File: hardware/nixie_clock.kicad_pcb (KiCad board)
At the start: 2 copper layers, 224 x 70 mm, 98 parts, among them J1 Conn_02x02_Odd_Even, J2 USB_C_Receptacle_USB2.0_16P, J7 Barrel_Jack_Switch, Q1 IRF740, Q2 BSS138, Q3 BSS138, Q4 BSS138, Q5 BSS138, Q6 BSS138, Q8 BSS138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

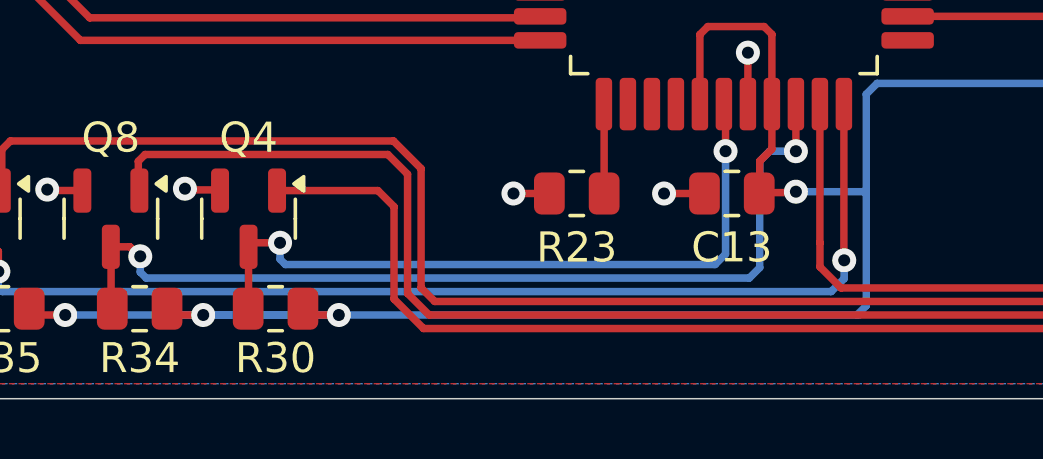
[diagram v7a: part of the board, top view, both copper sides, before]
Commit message: Correct track near U5.
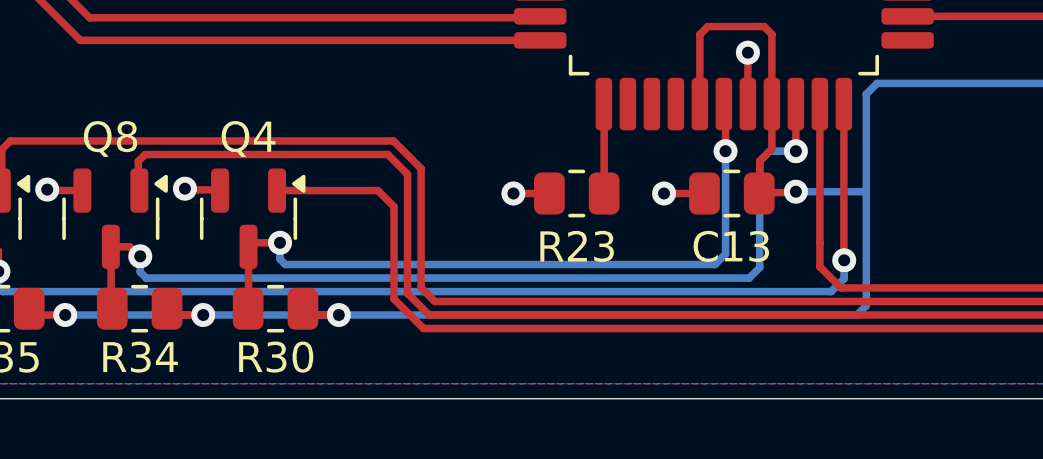
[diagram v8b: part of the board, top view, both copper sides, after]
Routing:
- net /connectors/12V: track 422.0 -> 416.7 mm
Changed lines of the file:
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@@
 	)
 	(segment
-		(start 96.039792 68.4625)
-		(end 96.039792 61.527708)
+		(start 103.41 127.21)
+		(end 86.14 127.21)
 		(width 0.25)
 		(layer "B.Cu")
@@
 	)
 	(segment
-		(start 103.5 127.21)
-		(end 80.97 127.21)
+		(start 96.039792 68.4625)
+		(end 96.039792 61.527708)
 		(width 0.25)
 		(layer "B.Cu")
@@
 		(min_thickness 0.25)
 		(filled_areas_thickness no)
-		(fill yes
+		(fill
 			(thermal_gap 0.5)
 			(thermal_bridge_width 0.5)
@@
 		(min_thickness 0.25)
 		(filled_areas_thickness no)
-		(fill yes
+		(fill
 			(thermal_gap 0.5)
 			(thermal_bridge_width 0.5)
